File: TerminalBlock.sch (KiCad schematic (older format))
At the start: 0 parts

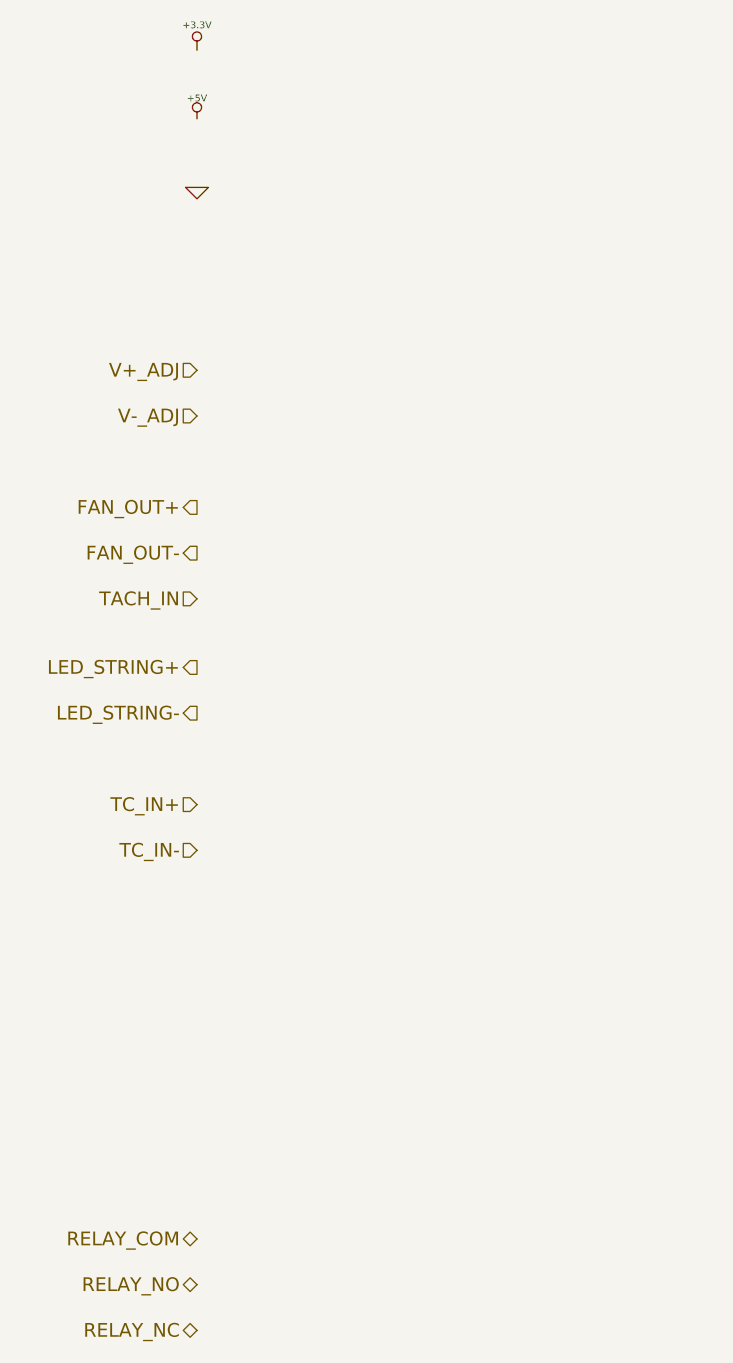
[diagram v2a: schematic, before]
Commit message: Associated and placed the terminal blocks and ATX header
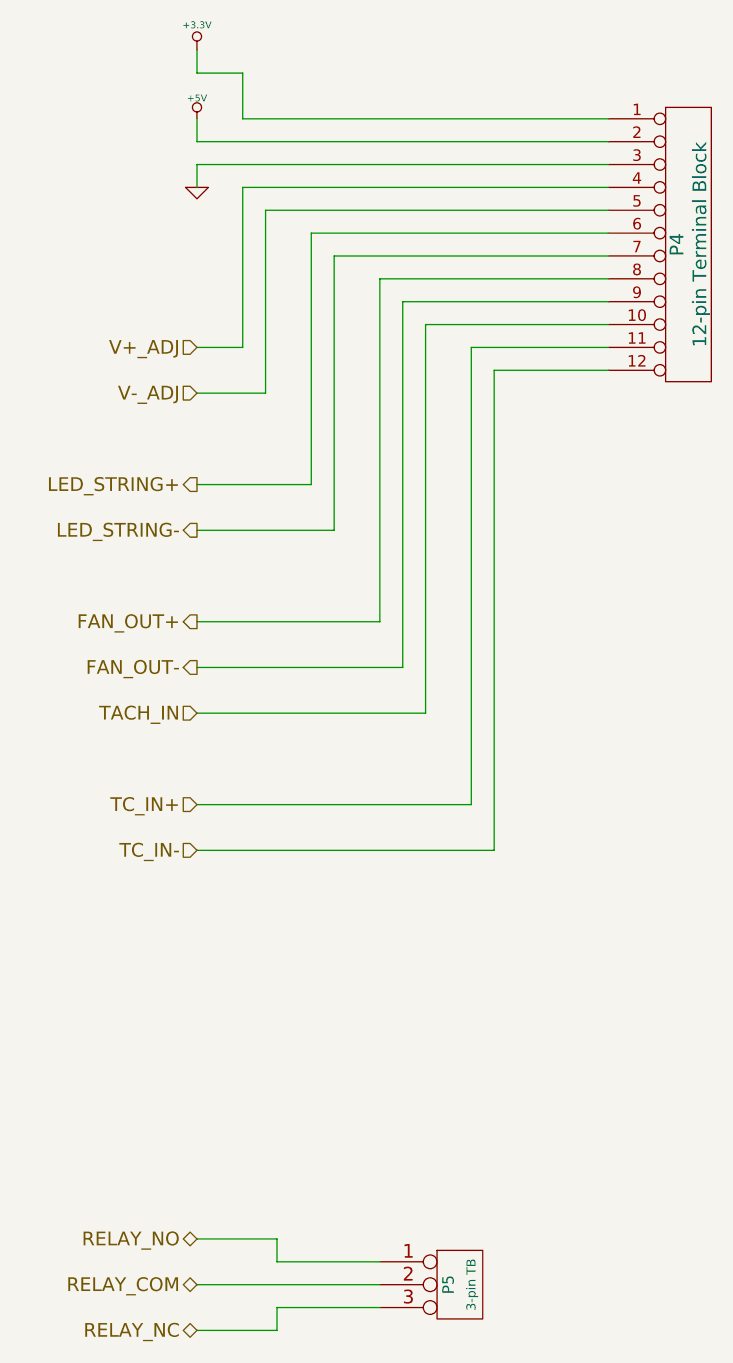
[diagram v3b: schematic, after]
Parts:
- added P4: 12-pin Terminal Block, symbol CONN_12
- added P5: 3-pin TB, symbol CONN_3
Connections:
- net +3.3V: now also P4.1 (P1)
- net +5V: now also P4.2 (P2)
- net FAN_OUT+: now also P4.8 (P8)
- net FAN_OUT-: now also P4.9 (P9)
- net GND: now also P4.3 (P3)
- net LED_STRING+: now also P4.6 (P6)
- net LED_STRING-: now also P4.7 (P7)
- net RELAY_COM: now also P5.2 (PM)
- net RELAY_NC: now also P5.3 (P3)
- net RELAY_NO: now also P5.1 (P1)
- net TACH_IN: now also P4.10 (P10)
- net TC_IN+: now also P4.11 (P11)
- net TC_IN-: now also P4.12 (P12)
- net V+_ADJ: now also P4.4 (P4)
- net V-_ADJ: now also P4.5 (P5)
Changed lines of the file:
@@
 $Descr A4 11693 8268
 encoding utf-8
-Sheet 6 9
+Sheet 5 9
 Title ""
 Date ""
@@
 Comment4 ""
 $EndDescr
-Text HLabel 2200 2400 0    60   Input ~ 0
+Text HLabel 2200 2300 0    60   Input ~ 0
 V+_ADJ
-Text HLabel 2200 2600 0    60   Input ~ 0
+Text HLabel 2200 2500 0    60   Input ~ 0
 V-_ADJ
-Text HLabel 2200 3000 0    60   Output ~ 0
+Text HLabel 2200 3500 0    60   Output ~ 0
 FAN_OUT+
-Text HLabel 2200 3200 0    60   Output ~ 0
+Text HLabel 2200 3700 0    60   Output ~ 0
 FAN_OUT-
-Text HLabel 2200 3400 0    60   Input ~ 0
+Text HLabel 2200 3900 0    60   Input ~ 0
 TACH_IN
-Text HLabel 2200 3700 0    60   Output ~ 0
+Text HLabel 2200 2900 0    60   Output ~ 0
 LED_STRING+
-Text HLabel 2200 3900 0    60   Output ~ 0
+Text HLabel 2200 3100 0    60   Output ~ 0
 LED_STRING-
 Text HLabel 2200 4300 0    60   Input ~ 0
@@
 Text HLabel 2200 4500 0    60   Input ~ 0
 TC_IN-
+Text HLabel 2200 6400 0    60   BiDi ~ 0
+RELAY_COM
 Text HLabel 2200 6200 0    60   BiDi ~ 0
-RELAY_COM
-Text HLabel 2200 6400 0    60   BiDi ~ 0
 RELAY_NO
 Text HLabel 2200 6600 0    60   BiDi ~ 0
@@
 	1    0    0    -1
 $EndComp
+$Comp
+L CONN_12 P4
+U 1 1 5308C0F9
+P 4350 1850
+F 0 "P4" V 4300 1850 60  0000 C CNN
+F 1 "12-pin Terminal Block" V 4400 1850 60  0000 C CNN
+F 2 "" H 4350 1850 60  0000 C CNN
+F 3 "" H 4350 1850 60  0000 C CNN
+F 4 "On Shore" H 4350 1850 60  0001 C CNN "MFG Name"
+F 5 "OSTTE120104" H 4350 1850 60  0001 C CNN "MFG Part Number"
+	1    4350 1850
+	1    0    0    -1
+$EndComp
+$Comp
+L CONN_3 P5
+U 1 1 5308C10D
+P 3350 6400
+F 0 "P5" V 3300 6400 50  0000 C CNN
+F 1 "3-pin TB" V 3400 6400 40  0000 C CNN
+F 2 "" H 3350 6400 60  0000 C CNN
+F 3 "" H 3350 6400 60  0000 C CNN
+F 4 "Phoenix" H 3350 6400 60  0001 C CNN "MFG Name"
+F 5 "1935174" H 3350 6400 60  0001 C CNN "MFG Part Number"
+	1    3350 6400
+	1    0    0    -1
+$EndComp
+Wire Wire Line
+	3100 2100 4000 2100
+Wire Wire Line
+	3100 3700 3100 2100
+Wire Wire Line
+	2200 3700 3100 3700
+Wire Wire Line
+	3000 2000 4000 2000
+Wire Wire Line
+	3000 3500 3000 2000
+Wire Wire Line
+	2200 3500 3000 3500
+Wire Wire Line
+	2800 1900 4000 1900
+Wire Wire Line
+	2800 3100 2800 1900
+Wire Wire Line
+	2200 3100 2800 3100
+Wire Wire Line
+	2700 1800 4000 1800
+Wire Wire Line
+	2700 2900 2700 1800
+Wire Wire Line
+	2200 2900 2700 2900
+Wire Wire Line
+	2500 1700 4000 1700
+Wire Wire Line
+	2500 2500 2500 1700
+Wire Wire Line
+	2200 2500 2500 2500
+Wire Wire Line
+	2400 1600 4000 1600
+Wire Wire Line
+	2400 2300 2400 1600
+Wire Wire Line
+	2200 2300 2400 2300
+Wire Wire Line
+	2200 1500 4000 1500
+Wire Wire Line
+	2200 1600 2200 1500
+Wire Wire Line
+	2200 1400 4000 1400
+Wire Wire Line
+	2200 1300 2200 1400
+Wire Wire Line
+	2400 1300 4000 1300
+Wire Wire Line
+	2400 1100 2400 1300
+Wire Wire Line
+	2200 1100 2400 1100
+Wire Wire Line
+	2200 1000 2200 1100
+Wire Wire Line
+	2200 3900 3200 3900
+Wire Wire Line
+	3200 3900 3200 2200
+Wire Wire Line
+	3200 2200 4000 2200
+Wire Wire Line
+	2200 4300 3400 4300
+Wire Wire Line
+	3400 4300 3400 2300
+Wire Wire Line
+	3400 2300 4000 2300
+Wire Wire Line
+	2200 4500 3500 4500
+Wire Wire Line
+	3500 4500 3500 2400
+Wire Wire Line
+	3500 2400 4000 2400
+Wire Wire Line
+	3000 6300 2550 6300
+Wire Wire Line
+	2550 6300 2550 6200
+Wire Wire Line
+	2550 6200 2200 6200
+Wire Wire Line
+	2200 6400 3000 6400
+Wire Wire Line
+	2200 6600 2550 6600
+Wire Wire Line
+	2550 6600 2550 6500
+Wire Wire Line
+	2550 6500 3000 6500
 $EndSCHEMATC

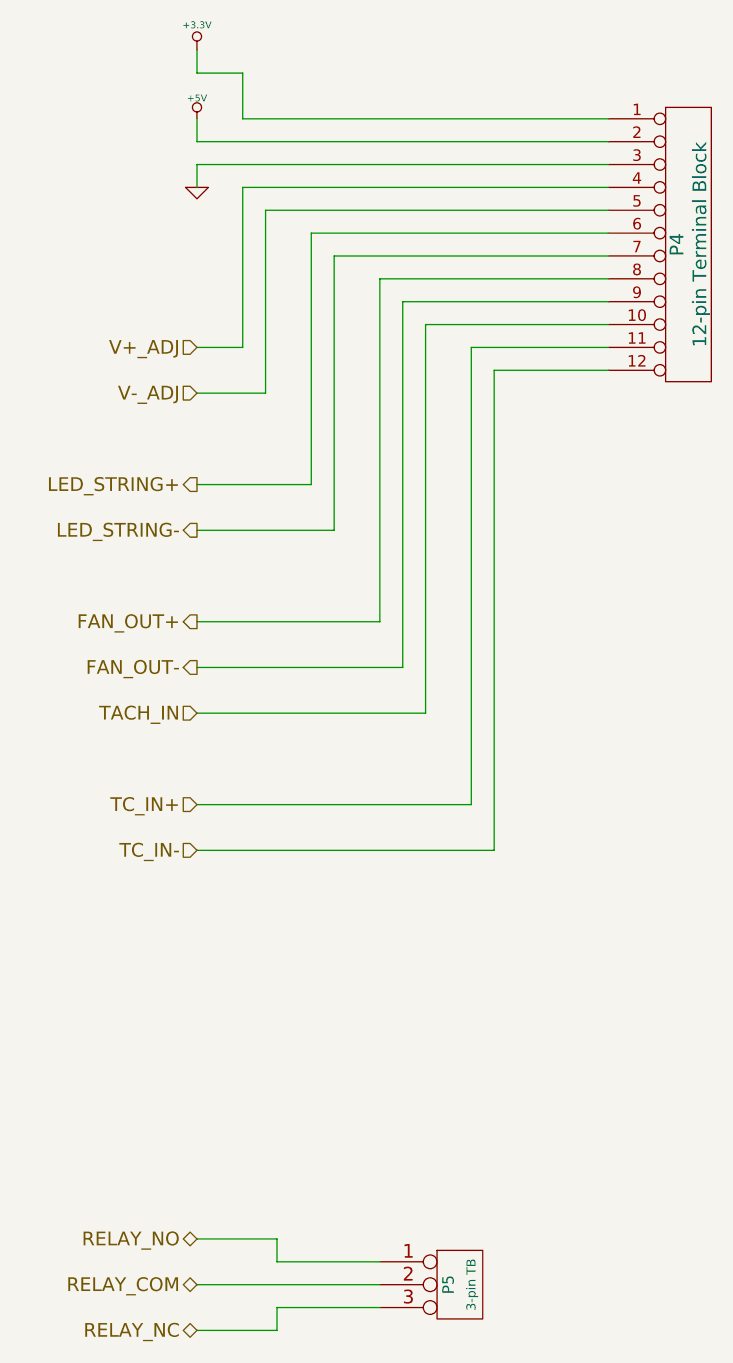
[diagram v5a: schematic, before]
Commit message: Various minor updates after Ground and Power Planes video
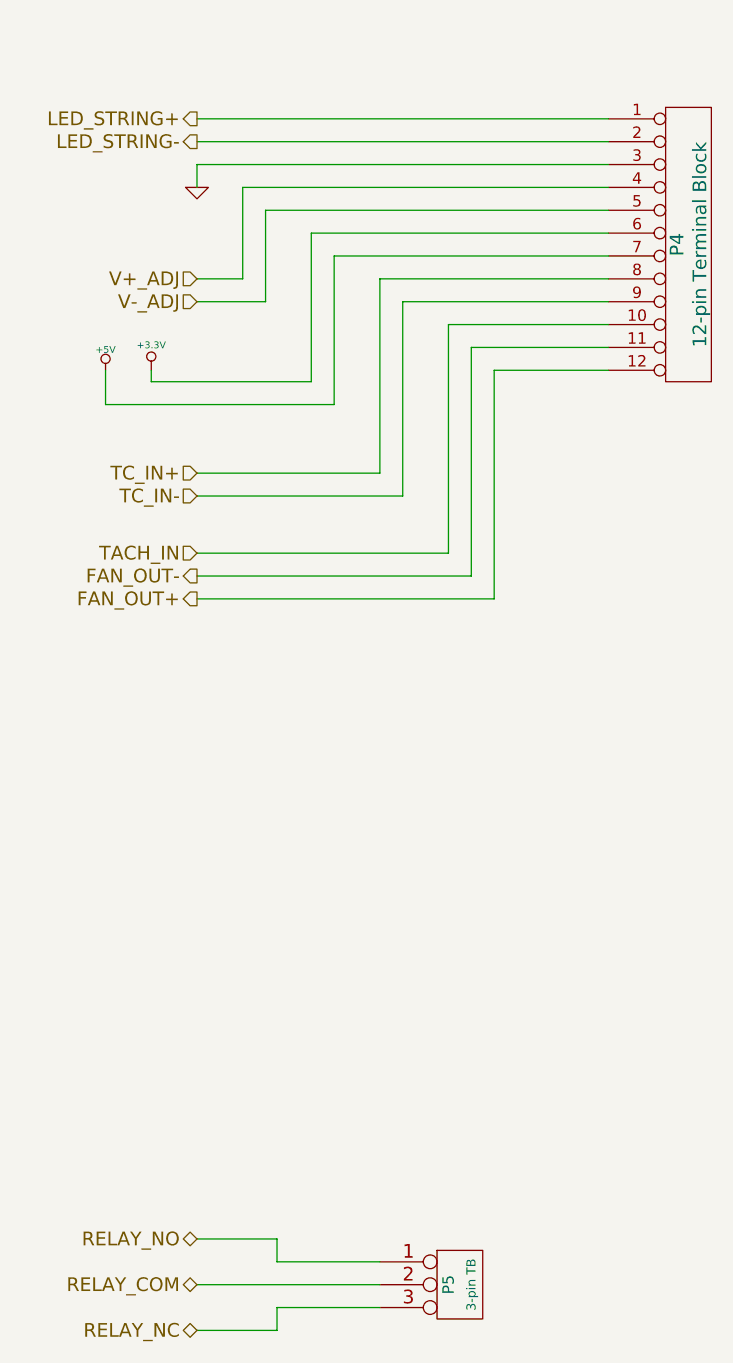
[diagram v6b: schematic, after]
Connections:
- net +3.3V: now also P4.6 (P6); no longer P4.1 (P1)
- net +5V: now also P4.7 (P7); no longer P4.2 (P2)
- net FAN_OUT+: now also P4.12 (P12); no longer P4.8 (P8)
- net FAN_OUT-: now also P4.11 (P11); no longer P4.9 (P9)
- net LED_STRING+: now also P4.1 (P1); no longer P4.6 (P6)
- net LED_STRING-: now also P4.2 (P2); no longer P4.7 (P7)
- net TC_IN+: now also P4.8 (P8); no longer P4.11 (P11)
- net TC_IN-: now also P4.9 (P9); no longer P4.12 (P12)
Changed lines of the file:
@@
 Comment4 ""
 $EndDescr
-Text HLabel 2200 2300 0    60   Input ~ 0
+Text HLabel 2200 2000 0    60   Input ~ 0
 V+_ADJ
-Text HLabel 2200 2500 0    60   Input ~ 0
+Text HLabel 2200 2100 0    60   Input ~ 0
 V-_ADJ
-Text HLabel 2200 3500 0    60   Output ~ 0
+Text HLabel 2200 3400 0    60   Output ~ 0
 FAN_OUT+
-Text HLabel 2200 3700 0    60   Output ~ 0
+Text HLabel 2200 3300 0    60   Output ~ 0
 FAN_OUT-
-Text HLabel 2200 3900 0    60   Input ~ 0
+Text HLabel 2200 3200 0    60   Input ~ 0
 TACH_IN
-Text HLabel 2200 2900 0    60   Output ~ 0
+Text HLabel 2200 1300 0    60   Output ~ 0
 LED_STRING+
-Text HLabel 2200 3100 0    60   Output ~ 0
+Text HLabel 2200 1400 0    60   Output ~ 0
 LED_STRING-
-Text HLabel 2200 4300 0    60   Input ~ 0
+Text HLabel 2200 2850 0    60   Input ~ 0
 TC_IN+
-Text HLabel 2200 4500 0    60   Input ~ 0
+Text HLabel 2200 2950 0    60   Input ~ 0
 TC_IN-
 Text HLabel 2200 6400 0    60   BiDi ~ 0
@@
 RELAY_NC
 $Comp
-L +3.3V #PWR022
+L +3.3V #PWR24
 U 1 1 52FC1D46
-P 2200 1000
-F 0 "#PWR022" H 2200 960 30  0001 C CNN
-F 1 "+3.3V" H 2200 1110 30  0000 C CNN
-F 2 "" H 2200 1000 60  0000 C CNN
-F 3 "" H 2200 1000 60  0000 C CNN
-	1    2200 1000
+P 2000 2400
+F 0 "#PWR24" H 2000 2360 30  0001 C CNN
+F 1 "+3.3V" H 2000 2510 30  0000 C CNN
+F 2 "" H 2000 2400 60  0000 C CNN
+F 3 "" H 2000 2400 60  0000 C CNN
+	1    2000 2400
 	1    0    0    -1
 $EndComp
 $Comp
-L +5V #PWR023
+L +5V #PWR23
 U 1 1 52FC1D5A
-P 2200 1300
-F 0 "#PWR023" H 2200 1390 20  0001 C CNN
-F 1 "+5V" H 2200 1390 30  0000 C CNN
-F 2 "" H 2200 1300 60  0000 C CNN
-F 3 "" H 2200 1300 60  0000 C CNN
-	1    2200 1300
+P 1800 2400
+F 0 "#PWR23" H 1800 2490 20  0001 C CNN
+F 1 "+5V" H 1800 2490 30  0000 C CNN
+F 2 "" H 1800 2400 60  0000 C CNN
+F 3 "" H 1800 2400 60  0000 C CNN
+	1    1800 2400
 	1    0    0    -1
 $EndComp
 $Comp
-L GND #PWR024
+L GND #PWR25
 U 1 1 52FC1D6E
 P 2200 1600
-F 0 "#PWR024" H 2200 1600 30  0001 C CNN
+F 0 "#PWR25" H 2200 1600 30  0001 C CNN
 F 1 "GND" H 2200 1530 30  0001 C CNN
 F 2 "" H 2200 1600 60  0000 C CNN
@@
 	3100 2100 4000 2100
 Wire Wire Line
-	3100 3700 3100 2100
+	3100 2950 3100 2100
 Wire Wire Line
-	2200 3700 3100 3700
+	2200 2950 3100 2950
 Wire Wire Line
 	3000 2000 4000 2000
 Wire Wire Line
-	3000 3500 3000 2000
+	3000 2850 3000 2000
 Wire Wire Line
-	2200 3500 3000 3500
+	2200 2850 3000 2850
 Wire Wire Line
 	2800 1900 4000 1900
 Wire Wire Line
-	2800 3100 2800 1900
+	2800 2550 2800 1900
 Wire Wire Line
-	2200 3100 2800 3100
+	2200 2100 2500 2100
 Wire Wire Line
 	2700 1800 4000 1800
 Wire Wire Line
-	2700 2900 2700 1800
+	2700 2450 2700 1800
 Wire Wire Line
-	2200 2900 2700 2900
+	2200 2000 2400 2000
 Wire Wire Line
 	2500 1700 4000 1700
 Wire Wire Line
-	2500 2500 2500 1700
+	2500 2100 2500 1700
 Wire Wire Line
-	2200 2500 2500 2500
+	1800 2550 2800 2550
 Wire Wire Line
 	2400 1600 4000 1600
 Wire Wire Line
-	2400 2300 2400 1600
+	2400 2000 2400 1600
 Wire Wire Line
-	2200 2300 2400 2300
+	2000 2450 2700 2450
 Wire Wire Line
 	2200 1500 4000 1500
@@
 	2200 1400 4000 1400
 Wire Wire Line
-	2200 1300 2200 1400
+	2200 1300 4000 1300
 Wire Wire Line
-	2400 1300 4000 1300
+	2000 2400 2000 2450
 Wire Wire Line
-	2400 1100 2400 1300
+	2200 3200 3300 3200
 Wire Wire Line
-	2200 1100 2400 1100
+	3300 3200 3300 2200
 Wire Wire Line
-	2200 1000 2200 1100
+	3300 2200 4000 2200
 Wire Wire Line
-	2200 3900 3200 3900
+	2200 3300 3400 3300
 Wire Wire Line
-	3200 3900 3200 2200
-Wire Wire Line
-	3200 2200 4000 2200
-Wire Wire Line
-	2200 4300 3400 4300
-Wire Wire Line
-	3400 4300 3400 2300
+	3400 3300 3400 2300
 Wire Wire Line
 	3400 2300 4000 2300
 Wire Wire Line
-	2200 4500 3500 4500
+	2200 3400 3500 3400
 Wire Wire Line
-	3500 4500 3500 2400
+	3500 3400 3500 2400
 Wire Wire Line
 	3500 2400 4000 2400
@@
 Wire Wire Line
 	2550 6500 3000 6500
+Wire Wire Line
+	1800 2400 1800 2550
 $EndSCHEMATC
